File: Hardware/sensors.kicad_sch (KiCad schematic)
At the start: 55 parts, among them IC5 ADS131M04IRUKR, J3 Rotary Pot, J4 Conn_01x02_Male, J5 1053131104, J6 1053131104, J7 Conn_01x02_Male, J8 Conn_01x02_Male, U10 MAX31856, U11 MAX31856, U9 THVD2429

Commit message: removed voltage pt sensing capabilities
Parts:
- removed J5, J6: 1053131104, Connector_Molex:Molex_Nano-Fit_105313-xx04_1x04_P2.50mm_Horizontal, symbol iclr:1053131104
- removed JP10, JP11, JP12, JP20, JP3, JP6: SolderJumper_3_Open, Jumper:SolderJumper-3_P1.3mm_Open_RoundedPad1.0x1.5mm_NumberLabels, symbol Jumper:SolderJumper_3_Open
- removed JP15, JP16, JP19, JP8: SolderJumper_2_Open, iclr:SmallerSolderJP, symbol Jumper:SolderJumper_2_Open
- removed R70, R79: 10k, Resistor_SMD:R_0402_1005Metric, symbol Device:R_Small
- removed R77: 75k, Resistor_SMD:R_0402_1005Metric, symbol Device:R_Small
- removed R78: 14k, Resistor_SMD:R_0402_1005Metric, symbol Device:R_Small
- removed R83, R87: 1k, Resistor_SMD:R_0402_1005Metric, symbol Device:R_Small
- removed R85: 49.9, Resistor_SMD:R_0402_1005Metric, symbol Device:R_Small
- added J5, J9: Conn_01x02_Male, Connector_Molex:Molex_Nano-Fit_105313-xx02_1x02_P2.50mm_Horizontal, symbol Connector:Conn_01x02_Male
- added R67: 59, Resistor_SMD:R_0402_1005Metric, symbol Device:R_Small
- R68: value 75k -> 1k; MPN RT0402BRD0775KL -> (none)
- R69: value 14k -> 1k; MPN 0402WGF1402TCE -> (none)
- R74: value 49.9 -> 59
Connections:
- net +12V: now also J5.1 (Pin_1), J9.1 (Pin_1)
- net AIN1N: now also R68.2
- net AIN1P: now also R69.2
- net GND: now also R68.1, R74.2, R76.1, R67.2
- net at R74.1: now also R72.1, J9.2 (Pin_2)
- net at R69.1: now also J5.2 (Pin_2), R67.1; no longer R68.2
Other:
- note added: "https://www.falstad.com/circuit/circuitjs.html?ctz=CQAgjCAMB0l3BWcMBMcUHYMGZIA4UA2ATmIxAUgpABZsKBTAWjDACgB3EQvPcFPgmIp+fSJ268QKGlSEiZVcQGMKw0WoWza4ZnxbQwebNhoyMNQnDCUaUWJAjiuJwtzuuN4gE6aNNPCowAShkODYAZWkMBXxorSVwEAAzAEMAGwBnBlCUCWwEBOkpRSh8wultOiKfWjgQT2w0Buw3INlwrlLu7U9xAAdJPlKePmC+ekSweBm2ACUNQI1x0KptJESYBHn-MZDNuv5V+22otD5COxXL0Ig0rJyqPK6Y93iGkWcWtxvGz4kOm9AU0yl0EG4ek9tF9MCIbrDpHFak0qJ5Sn1JNNx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"
- note removed: "12V"
- note removed: "5V"
- note removed: "Current"
- note removed: "Jump for current"
- note removed: "Jump for voltage"
- note removed: "Voltage"
- moved on the sheet: C81, R72, R74, R76

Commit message: chatting to fang
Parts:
- IC5: footprint QFN40P300X300X80-21N-D -> iclr:QFN40P300X300X80-21N-D
- U9: footprint (none) -> iclr:TPS74901DRCR
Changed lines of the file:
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@@
 			)
 		)
-		(property "Footprint" ""
+		(property "Footprint" "iclr:TPS74901DRCR"
 			(at 74.93 41.91 0)
 			(effects
@@
 			)
 		)
-		(property "Footprint" "QFN40P300X300X80-21N-D"
+		(property "Footprint" "iclr:QFN40P300X300X80-21N-D"
 			(at 282.88 95.25 0)
 			(effects

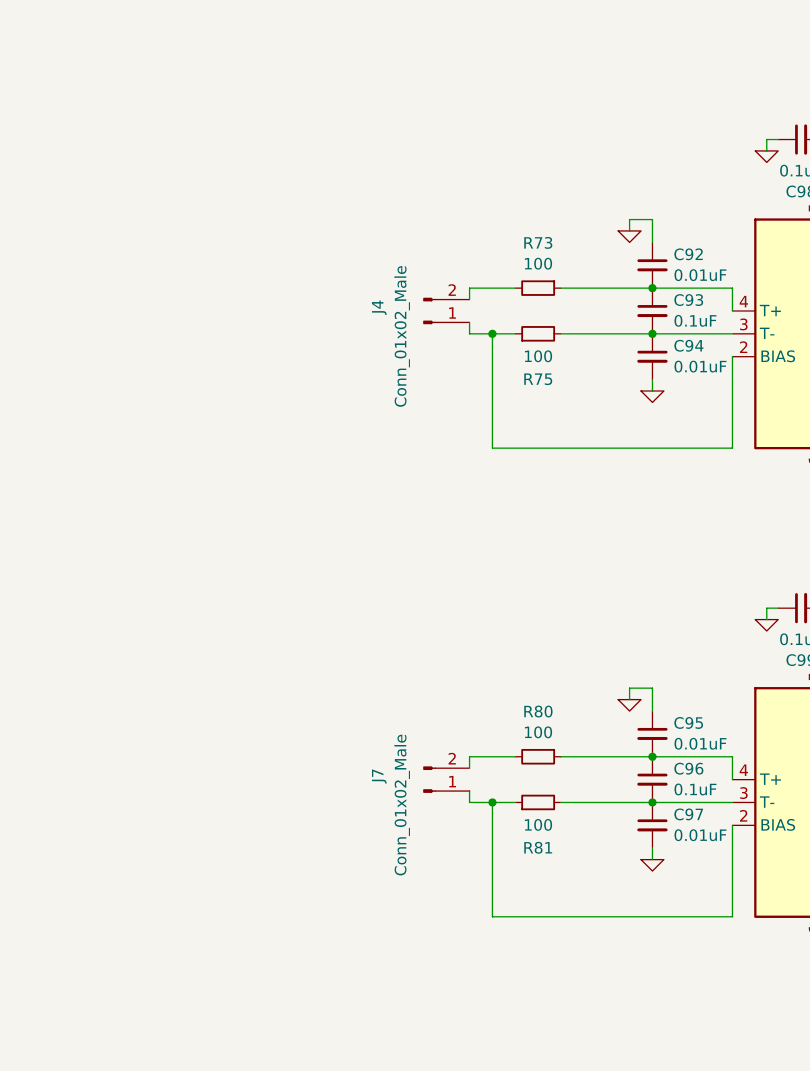
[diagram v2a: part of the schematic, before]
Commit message: updated settled pcb design
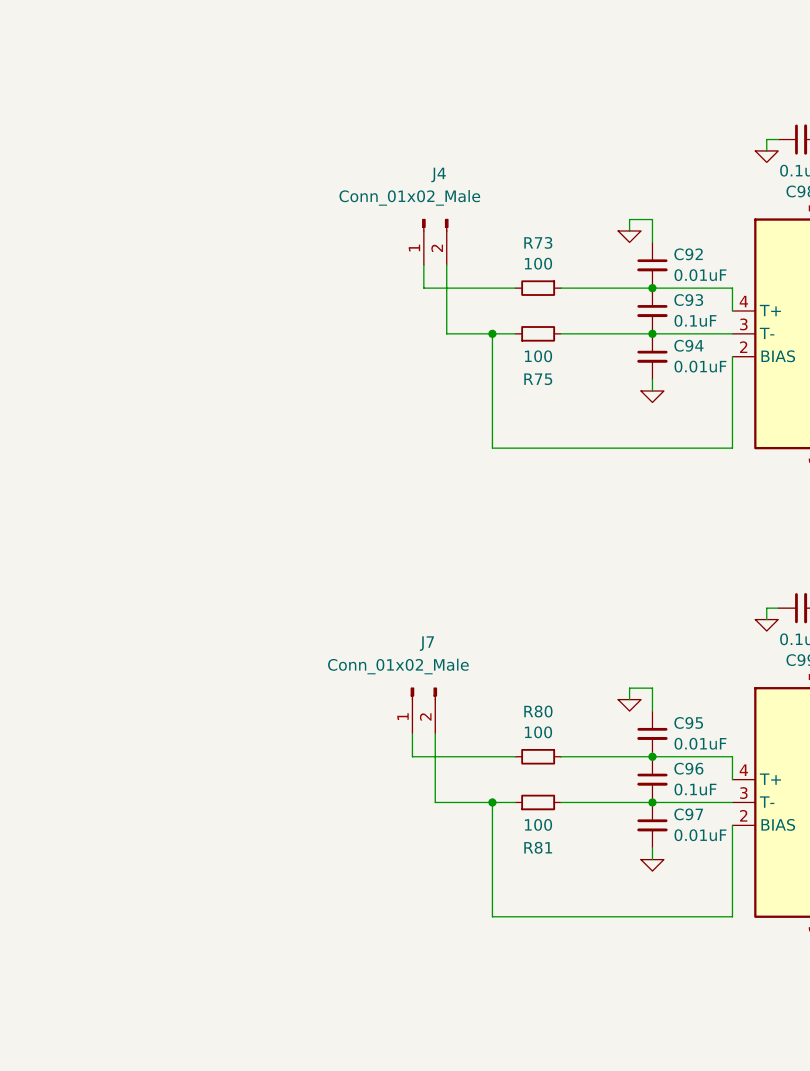
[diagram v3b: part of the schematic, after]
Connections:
- net at R73.2: now also J4.1 (Pin_1); no longer J4.2 (Pin_2)
- net at R80.2: now also J7.1 (Pin_1); no longer J7.2 (Pin_2)
- net at R75.1, U10.2 (BIAS): now also J4.2 (Pin_2); no longer J4.1 (Pin_1)
- net at R81.1, U11.2 (BIAS): now also J7.2 (Pin_2); no longer J7.1 (Pin_1)
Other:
- moved on the sheet: J4, J7
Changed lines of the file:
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@@
 	(wire
 		(pts
+			(xy 45.72 107.95) (xy 55.88 107.95)
+		)
+		(stroke
+			(width 0)
+			(type default)
+		)
+	)
+	(wire
+		(pts
 			(xy 229.87 44.45) (xy 238.76 44.45)
 		)
@@
 	(wire
 		(pts
+			(xy 46.99 165.1) (xy 53.34 165.1)
+		)
+		(stroke
+			(width 0)
+			(type default)
+		)
+	)
+	(wire
+		(pts
 			(xy 95.25 142.24) (xy 95.25 143.51)
 		)
@@
 	(wire
 		(pts
+			(xy 44.45 160.02) (xy 44.45 157.48)
+		)
+		(stroke
+			(width 0)
+			(type default)
+		)
+	)
+	(wire
+		(pts
 			(xy 92.71 180.34) (xy 95.25 180.34)
 		)
@@
 	(wire
 		(pts
-			(xy 50.8 113.03) (xy 53.34 113.03)
+			(xy 48.26 113.03) (xy 53.34 113.03)
 		)
 		(stroke
@@
 	(wire
 		(pts
-			(xy 254 57.15) (xy 254 53.34)
+			(xy 45.72 105.41) (xy 45.72 107.95)
 		)
 		(stroke
@@
 	(wire
 		(pts
-			(xy 55.88 107.95) (xy 50.8 107.95)
+			(xy 254 57.15) (xy 254 53.34)
 		)
 		(stroke
@@
 	(wire
 		(pts
-			(xy 50.8 111.76) (xy 50.8 113.03)
-		)
-		(stroke
-			(width 0)
-			(type default)
-		)
-	)
-	(wire
-		(pts
 			(xy 231.14 111.76) (xy 243.84 111.76)
 		)
@@
 	(wire
 		(pts
-			(xy 50.8 107.95) (xy 50.8 109.22)
-		)
-		(stroke
-			(width 0)
-			(type default)
-		)
-	)
-	(wire
-		(pts
 			(xy 60.96 160.02) (xy 71.12 160.02)
 		)
@@
 	(wire
 		(pts
-			(xy 50.8 163.83) (xy 50.8 165.1)
-		)
-		(stroke
-			(width 0)
-			(type default)
-		)
-	)
-	(wire
-		(pts
 			(xy 71.12 160.02) (xy 80.01 160.02)
 		)
@@
 	(wire
 		(pts
-			(xy 55.88 160.02) (xy 50.8 160.02)
-		)
-		(stroke
-			(width 0)
-			(type default)
-		)
-	)
-	(wire
-		(pts
 			(xy 168.91 44.45) (xy 168.91 45.72)
 		)
@@
 	(wire
 		(pts
-			(xy 50.8 165.1) (xy 53.34 165.1)
+			(xy 46.99 165.1) (xy 46.99 157.48)
 		)
 		(stroke
@@
 	(wire
 		(pts
+			(xy 48.26 105.41) (xy 48.26 113.03)
+		)
+		(stroke
+			(width 0)
+			(type default)
+		)
+	)
+	(wire
+		(pts
 			(xy 171.45 101.6) (xy 175.26 101.6)
 		)
@@
 	(wire
 		(pts
-			(xy 254 44.45) (xy 248.92 44.45)
+			(xy 55.88 160.02) (xy 44.45 160.02)
 		)
 		(stroke
@@
 	(wire
 		(pts
-			(xy 95.25 91.44) (xy 95.25 97.79)
+			(xy 254 44.45) (xy 248.92 44.45)
 		)
 		(stroke
@@
 	(wire
 		(pts
-			(xy 90.17 91.44) (xy 90.17 90.17)
+			(xy 95.25 91.44) (xy 95.25 97.79)
 		)
 		(stroke
@@
 	(wire
 		(pts
-			(xy 166.37 107.95) (xy 166.37 109.22)
+			(xy 90.17 91.44) (xy 90.17 90.17)
 		)
 		(stroke
@@
 	(wire
 		(pts
-			(xy 46.99 44.45) (xy 46.99 45.72)
+			(xy 166.37 107.95) (xy 166.37 109.22)
 		)
 		(stroke
@@
 	(wire
 		(pts
-			(xy 245.11 143.51) (xy 252.73 143.51)
+			(xy 46.99 44.45) (xy 46.99 45.72)
 		)
 		(stroke
@@
 	(wire
 		(pts
-			(xy 203.2 125.73) (xy 203.2 121.92)
+			(xy 245.11 143.51) (xy 252.73 143.51)
 		)
 		(stroke
@@
 	(wire
 		(pts
-			(xy 71.12 118.11) (xy 71.12 119.38)
+			(xy 203.2 125.73) (xy 203.2 121.92)
 		)
 		(stroke
@@
 	(wire
 		(pts
-			(xy 50.8 160.02) (xy 50.8 161.29)
+			(xy 71.12 118.11) (xy 71.12 119.38)
 		)
 		(stroke
@@
 	(symbol
 		(lib_id "Connector:Conn_01x02_Male")
-		(at 45.72 111.76 0)
+		(at 45.72 100.33 90)
 		(mirror x)
 		(unit 1)
@@
 		(dnp no)
 		(property "Reference" "J4"
-			(at 40.64 109.22 90)
+			(at 48.26 95.25 90)
 			(effects
 				(font
@@
 		)
 		(property "Value" "Conn_01x02_Male"
-			(at 43.18 105.41 90)
+			(at 52.07 97.79 90)
 			(effects
 				(font
@@
 		)
 		(property "Footprint" "Connector_Molex:Molex_Nano-Fit_105313-xx02_1x02_P2.50mm_Horizontal"
-			(at 45.72 111.76 0)
+			(at 45.72 100.33 0)
 			(effects
 				(font
@@
 		)
 		(property "Datasheet" "~"
-			(at 45.72 111.76 0)
+			(at 45.72 100.33 0)
 			(effects
 				(font
@@
 		)
 		(property "Description" ""
-			(at 45.72 111.76 0)
+			(at 45.72 100.33 0)
 			(effects
 				(font
@@
 	(symbol
 		(lib_id "Connector:Conn_01x02_Male")
-		(at 45.72 163.83 0)
+		(at 44.45 152.4 90)
 		(mirror x)
 		(unit 1)
@@
 		(dnp no)
 		(property "Reference" "J7"
-			(at 40.64 161.29 90)
+			(at 46.99 147.32 90)
 			(effects
 				(font
@@
 		)
 		(property "Value" "Conn_01x02_Male"
-			(at 43.18 157.48 90)
+			(at 50.8 149.86 90)
 			(effects
 				(font
@@
 		)
 		(property "Footprint" "Connector_Molex:Molex_Nano-Fit_105313-xx02_1x02_P2.50mm_Horizontal"
-			(at 45.72 163.83 0)
+			(at 44.45 152.4 0)
 			(effects
 				(font
@@
 		)
 		(property "Datasheet" "~"
-			(at 45.72 163.83 0)
+			(at 44.45 152.4 0)
 			(effects
 				(font
@@
 		)
 		(property "Description" ""
-			(at 45.72 163.83 0)
+			(at 44.45 152.4 0)
 			(effects
 				(font

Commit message: final touches and adding encoder
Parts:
- removed J3: Rotary Pot, iclr:Molex_Nano-Fit_105313-xx03_1x03_P2.50mm_Horizontal, symbol Connector:Conn_01x03_Male
- removed R64: 8.56k, Resistor_SMD:R_0402_1005Metric, symbol Device:R_Small
- added J3: 3x2 Nanofit, 1053141206, symbol ICLR_HW:105314-1206
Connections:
- net GND: now also J3.4; no longer IC5.6 (AIN2N)
- net MISO: now also J3.2
- net MOSI: now also J3.3
- net SCLK: now also J3.1
- net VCC: now also J3.6
- net AIN2P: no longer names the net of IC5.5 (AIN2P)
- new net ENCODER_CS: J3.5
- no-connect marks 7 -> 9
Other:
- note removed: "SIM:"
- note removed: "https://www.falstad.com/circuit/circuitjs.html?ctz=CQAgjCAMB0l3BWcMBMcUHYMGZIA4UA2ATmIxAUgpABZsKBTAWjDACgAlEbBFcFPN14hCNKOJpVs0elTnQEbMBjE8+KBIW6FBuMREpwo0SRA4MAzgEsLAFwCGAOwDGDNgHMKhKpKqafNIJybAAOtKIgAoI0Eb7c4lRg8MlsAO7aglHhYlmQbNgYPhFZ-pF4uglsAE5eVCXetEZSyXnpMWJxpXF5NWrgGFp9KJLieP4eQnzYaJOzwQVSwmACs8qDlelDI0OaUGxAA"
- moved on the sheet: C77, C78, C79, IC5

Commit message: touching up and adding thermals for coating
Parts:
- J3: footprint 1053141206 -> Connector_Molex:Molex_Nano-Fit_105314-xx06_2x03_P2.50mm_Horizontal
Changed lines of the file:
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@@
 			)
 		)
-		(property "Footprint" "1053141206"
+		(property "Footprint" "Connector_Molex:Molex_Nano-Fit_105314-xx06_2x03_P2.50mm_Horizontal"
 			(at 228.6 243.51 0)
 			(effects

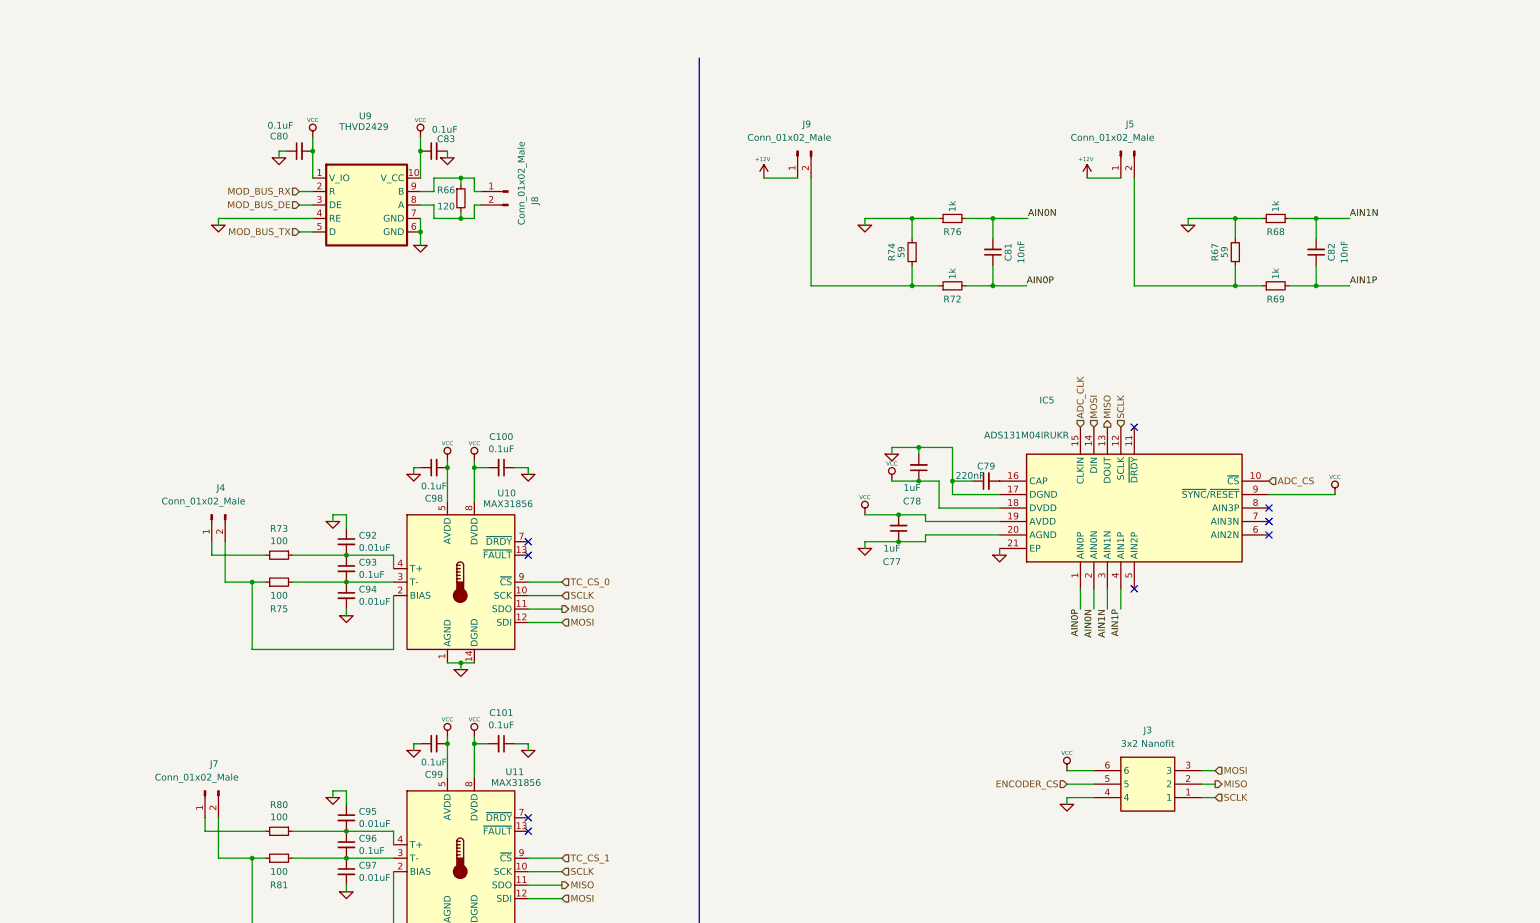
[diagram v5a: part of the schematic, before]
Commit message: added 2wire sensor and silkscreen
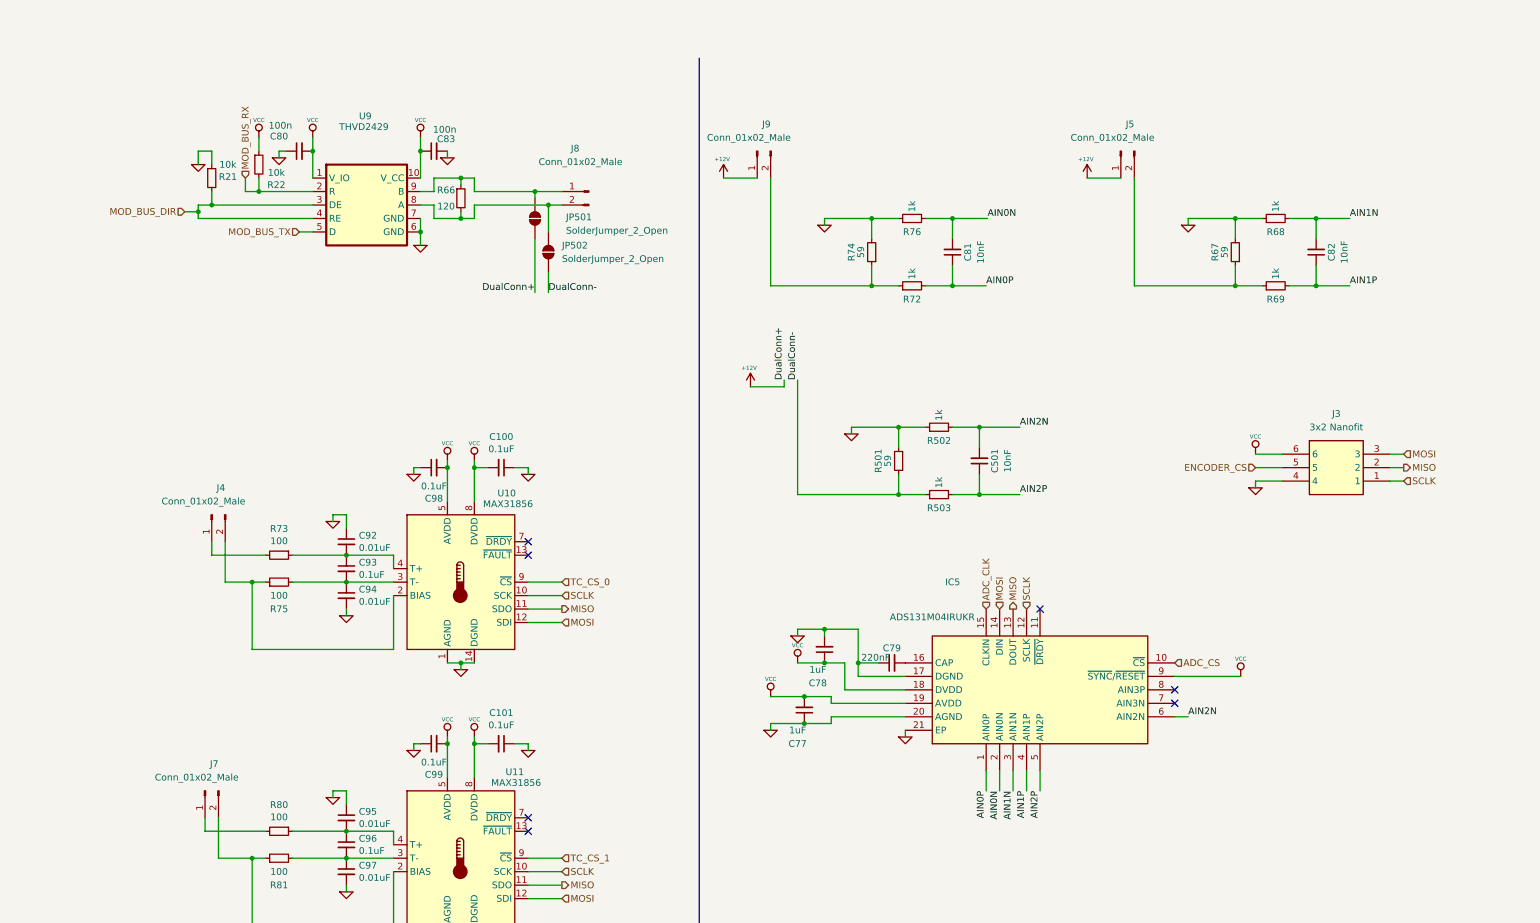
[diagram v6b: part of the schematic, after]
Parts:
- added C501: 10nF, Capacitor_SMD:C_0402_1005Metric, symbol Device:C_Small
- added JP501, JP502: SolderJumper_2_Open, iclr:small_2_pad_jumper_open, symbol Jumper:SolderJumper_2_Open
- added R21, R22: 10k, Resistor_SMD:R_0402_1005Metric, symbol Device:R_Small
- added R501: 59, Resistor_SMD:R_0402_1005Metric, symbol Device:R_Small
- added R502, R503: 1k, Resistor_SMD:R_0402_1005Metric, symbol Device:R_Small
- C80, C83: value 0.1uF -> 100n
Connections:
- net +12V: now also JP501.1 (A)
- net GND: now also R21.1, R501.2, R502.1; no longer U9.4 (RE)
- net MOD_BUS_RX: now also R22.2
- net VCC: now also R22.1
- net at J8.2 (Pin_2), R66.2, U9.8 (A): now also JP502.2 (B)
- net at J8.1 (Pin_1), R66.1, U9.9 (B): now also JP501.2 (B)
- net AIN2P: now reaches IC5.5 (AIN2P)
- net AIN2P: now also C501.1, R503.2
- net AIN2N: now reaches IC5.6 (AIN2N)
- net AIN2N: now also C501.2, R502.2
- net MOD_BUS_DE renamed MOD_BUS_DIR
- net MOD_BUS_DIR: now also U9.4 (RE), R21.2
- new net DualConn-: JP502.1 (A), R501.1, R503.1
- no-connect marks 9 -> 7
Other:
- moved on the sheet: C77, C78, C79, C81, IC5, J3, J8, J9, R72, R74, R76

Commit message: changes made post will's review
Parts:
- removed U9: THVD2429, iclr:TPS74901DRCR, symbol ICLR_HW:THVD2429
- added U501: THVD2429DRCR, easyeda2kicad:VSON-10_L3.0-W3.0-P0.50-BL-EP_DRC, symbol easyeda2kicad:THVD2429DRCR
- C501: renamed from C80; value 100n -> 100nF
- C502: renamed from C92; value 0.01uF -> 10nF
- C503: renamed from C93; value 0.1uF -> 100nF
- C504: renamed from C94; value 0.01uF -> 10nF
- C505: renamed from C95; value 0.01uF -> 10nF
- C506: renamed from C96; value 0.1uF -> 100nF
- C507: renamed from C97; value 0.01uF -> 10nF
- C508: renamed from C99; value 0.1uF -> 100nF
- C509: renamed from C98; value 0.1uF -> 100nF
- C510: renamed from C83; value 100n -> 100nF
- C511: renamed from C100; value 0.1uF -> 100nF
- C512: renamed from C101; value 0.1uF -> 100nF
- R501: renamed from R21; value 10k -> 10kΩ
- R502: renamed from R22; value 10k -> 10kΩ
- R503: renamed from R73; value 100 -> 100Ω
- R504: renamed from R75; value 100 -> 100Ω
- R505: renamed from R80; value 100 -> 100Ω
- R506: renamed from R81; value 100 -> 100Ω
- R507: renamed from R66; value 120 -> 120Ω
- R508: renamed from R74; value 59 -> 59Ω
- R509: renamed from R501; value 59 -> 59Ω
- R510: renamed from R76; value 1k -> 1kΩ
- R511: renamed from R72; value 1k -> 1kΩ
- R512: renamed from R502; value 1k -> 1kΩ
- R513: renamed from R503; value 1k -> 1kΩ
- R514: renamed from R67; value 59 -> 59Ω
- R515: renamed from R68; value 1k -> 1kΩ
- R516: renamed from R69; value 1k -> 1kΩ
- renumbered C77 to C513, C78 to C514, C79 to C515, C81 to C516, C501 to C517, C82 to C518, IC5 to IC501, J7 to J501, J4 to J502, J8 to J503, J9 to J504, J5 to J505, J3 to J506, U10 to U502, U11 to U503
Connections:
- net GND: now also U501.11 (EP), U501.6 (GND), U501.7 (GND)
- net MOD_BUS_DIR: now also U501.3 (DE), U501.4 (~{RE})
- net MOD_BUS_RX: now also U501.2 (R)
- net MOD_BUS_TX: now also U501.5 (D)
- net at J503.2 (Pin_2), JP502.2 (B), R507.2: now also U501.8 (A)
- net at J503.1 (Pin_1), JP501.2 (B), R507.1: now also U501.9 (B)
- net VCC renamed +3V3
- net +3V3: now also U501.1 (VIO), U501.10 (VCC)
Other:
- moved on the sheet: C501, C508, C510, C512, C514, R501, R502, R507
